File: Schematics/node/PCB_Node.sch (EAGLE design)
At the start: 30 parts, among them U1 ATMEGA328P, U2 MAX485CSA+, U3 MCP1824ST-3302E/DB, Y2 16MHz

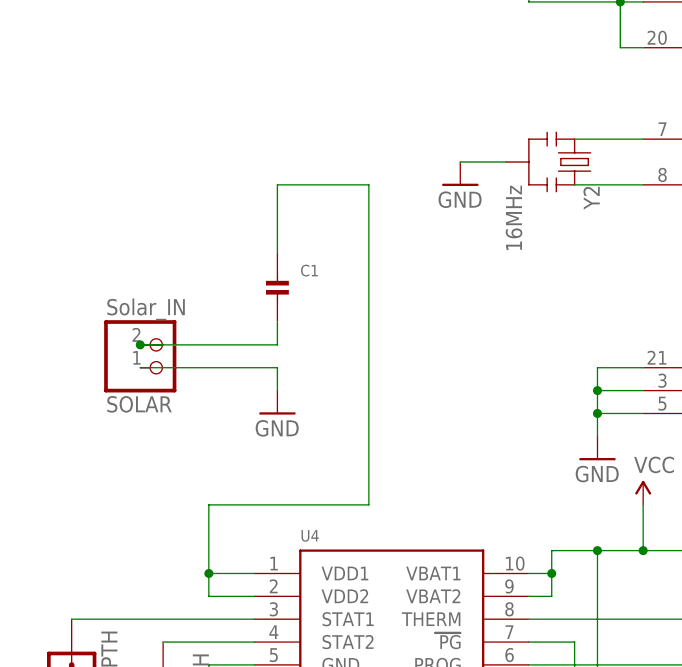
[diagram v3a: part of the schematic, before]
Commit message: Node fixes
Corrected the c1 capacitor connected to solar power correctly
moved part names to locations where they will be read because of vias
blocking them
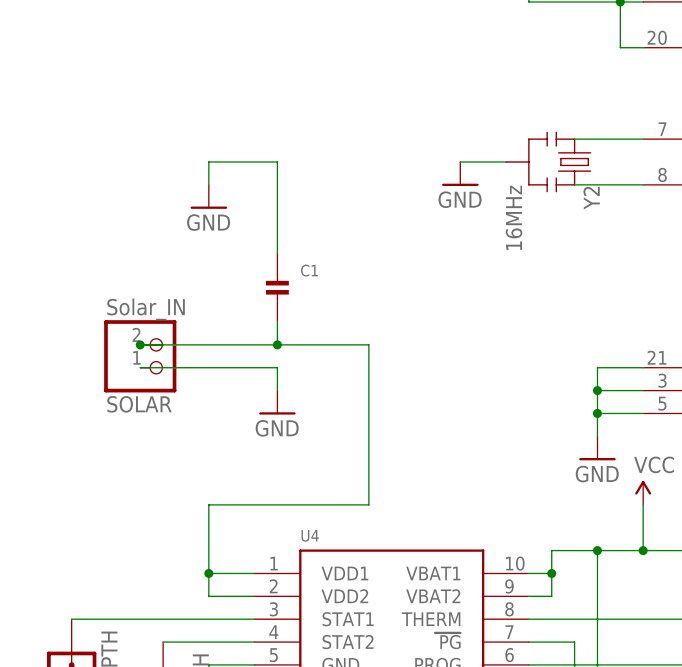
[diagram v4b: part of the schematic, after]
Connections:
- removed net N$14: C1.P$1, U4.VDD1, U4.VDD2
- net GND: now also C1.P$1
- net N$8: now also U4.VDD1, U4.VDD2
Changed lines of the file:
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@@
 <part name="JP12" library="SparkFun-Connectors" deviceset="M01" device="PTH"/>
 <part name="SUPPLY5" library="SparkFun-Aesthetics" deviceset="VCC" device=""/>
+<part name="GND13" library="SparkFun-Aesthetics" deviceset="GND" device=""/>
 </parts>
 <sheets>
@@
 <instance part="JP12" gate="G$1" x="-170.18" y="17.78" rot="R90"/>
 <instance part="SUPPLY5" gate="G$1" x="-116.84" y="40.64"/>
+<instance part="GND13" gate="1" x="-165.1" y="73.66"/>
 </instances>
 <busses>
@@
 <wire x1="-132.08" y1="78.74" x2="-137.16" y2="78.74" width="0.1524" layer="91"/>
 </segment>
+<segment>
+<pinref part="GND13" gate="1" pin="GND"/>
+<wire x1="-165.1" y1="76.2" x2="-165.1" y2="78.74" width="0.1524" layer="91"/>
+<pinref part="C1" gate="G$1" pin="P$1"/>
+<wire x1="-157.48" y1="68.58" x2="-157.48" y2="78.74" width="0.1524" layer="91"/>
+<wire x1="-165.1" y1="78.74" x2="-157.48" y2="78.74" width="0.1524" layer="91"/>
+</segment>
 </net>
 <net name="3" class="0">
@@
 <pinref part="SOLAR" gate="G$1" pin="2"/>
 <junction x="-172.72" y="58.42"/>
-</segment>
-</net>
-<net name="N$9" class="0">
-<segment>
-<pinref part="JP10" gate="G$1" pin="1"/>
-<pinref part="U4" gate="G$1" pin="STAT1"/>
-<wire x1="-180.34" y1="27.94" x2="-160.02" y2="27.94" width="0.1524" layer="91"/>
-</segment>
-</net>
-<net name="N$10" class="0">
-<segment>
-<pinref part="U4" gate="G$1" pin="STAT2"/>
-<pinref part="JP12" gate="G$1" pin="1"/>
-<wire x1="-160.02" y1="25.4" x2="-170.18" y2="25.4" width="0.1524" layer="91"/>
-</segment>
-</net>
-<net name="N$11" class="0">
-<segment>
-<pinref part="U4" gate="G$1" pin="PG"/>
-<wire x1="-129.54" y1="25.4" x2="-124.46" y2="25.4" width="0.1524" layer="91"/>
-<wire x1="-124.46" y1="25.4" x2="-124.46" y2="17.78" width="0.1524" layer="91"/>
-<wire x1="-124.46" y1="17.78" x2="-132.08" y2="17.78" width="0.1524" layer="91"/>
-<pinref part="JP11" gate="G$1" pin="1"/>
-<wire x1="-132.08" y1="17.78" x2="-132.08" y2="12.7" width="0.1524" layer="91"/>
-</segment>
-</net>
-<net name="N$14" class="0">
-<segment>
 <pinref part="U4" gate="G$1" pin="VDD2"/>
 <wire x1="-160.02" y1="30.48" x2="-165.1" y2="30.48" width="0.1524" layer="91"/>
@@
 <wire x1="-160.02" y1="33.02" x2="-165.1" y2="33.02" width="0.1524" layer="91"/>
 <junction x="-165.1" y="33.02"/>
-<pinref part="C1" gate="G$1" pin="P$1"/>
-<wire x1="-157.48" y1="68.58" x2="-157.48" y2="76.2" width="0.1524" layer="91"/>
-<wire x1="-157.48" y1="76.2" x2="-147.32" y2="76.2" width="0.1524" layer="91"/>
-<wire x1="-147.32" y1="76.2" x2="-147.32" y2="40.64" width="0.1524" layer="91"/>
 <wire x1="-147.32" y1="40.64" x2="-165.1" y2="40.64" width="0.1524" layer="91"/>
-</segment>
-</net>
+<wire x1="-157.48" y1="58.42" x2="-147.32" y2="58.42" width="0.1524" layer="91"/>
+<wire x1="-147.32" y1="58.42" x2="-147.32" y2="40.64" width="0.1524" layer="91"/>
+<junction x="-157.48" y="58.42"/>
+</segment>
+</net>
+<net name="N$9" class="0">
+<segment>
+<pinref part="JP10" gate="G$1" pin="1"/>
+<pinref part="U4" gate="G$1" pin="STAT1"/>
+<wire x1="-180.34" y1="27.94" x2="-160.02" y2="27.94" width="0.1524" layer="91"/>
+</segment>
+</net>
+<net name="N$10" class="0">
+<segment>
+<pinref part="U4" gate="G$1" pin="STAT2"/>
+<pinref part="JP12" gate="G$1" pin="1"/>
+<wire x1="-160.02" y1="25.4" x2="-170.18" y2="25.4" width="0.1524" layer="91"/>
+</segment>
+</net>
+<net name="N$11" class="0">
+<segment>
+<pinref part="U4" gate="G$1" pin="PG"/>
+<wire x1="-129.54" y1="25.4" x2="-124.46" y2="25.4" width="0.1524" layer="91"/>
+<wire x1="-124.46" y1="25.4" x2="-124.46" y2="17.78" width="0.1524" layer="91"/>
+<wire x1="-124.46" y1="17.78" x2="-132.08" y2="17.78" width="0.1524" layer="91"/>
+<pinref part="JP11" gate="G$1" pin="1"/>
+<wire x1="-132.08" y1="17.78" x2="-132.08" y2="12.7" width="0.1524" layer="91"/>
+</segment>
+</net>
